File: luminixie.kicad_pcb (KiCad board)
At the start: 2 copper layers, 162.6 x 50.8 mm, 31 parts, among them J1 Conn_01x03_Female, U1 ESP32-MINIKIT, U2 HV-POWER, U3 HV5530_PLCC, U4 HV5530_PLCC

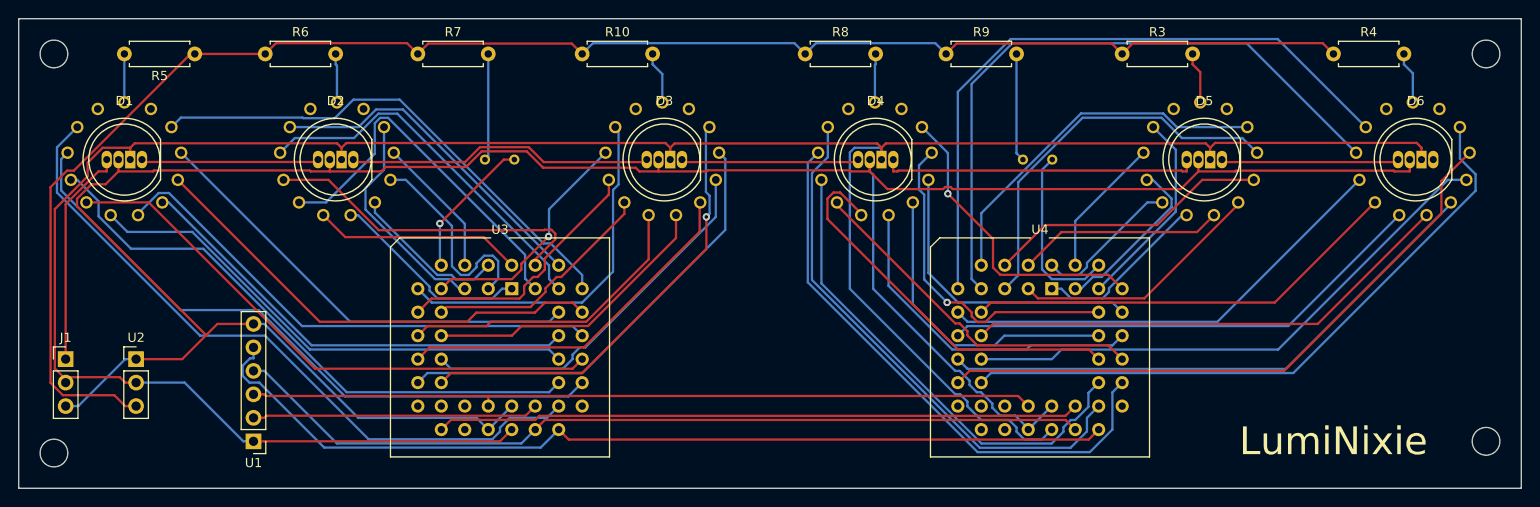
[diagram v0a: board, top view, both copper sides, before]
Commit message: Voltage divider for IN-3
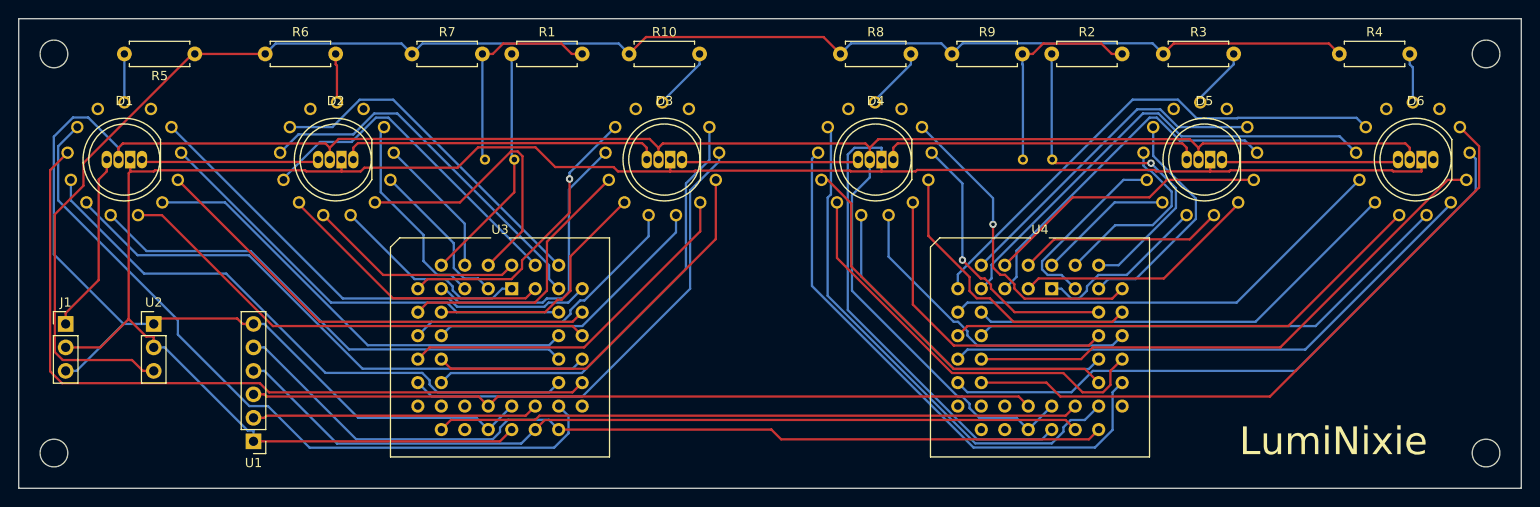
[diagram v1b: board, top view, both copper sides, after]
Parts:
- removed REF** (x4): MountingHole_3mm, MountingHole:MountingHole_3mm
- added R1: ?, Resistor_THT:R_Axial_DIN0207_L6.3mm_D2.5mm_P7.62mm_Horizontal, F.Cu at (133.3, 62.2)
- added R2: ?, Resistor_THT:R_Axial_DIN0207_L6.3mm_D2.5mm_P7.62mm_Horizontal, F.Cu at (191.8, 62.2)
- added REF1: MountingHole_3mm, MountingHole:MountingHole_3mm, F.Cu at (83.8, 62.2)
- added REF2: MountingHole_3mm, MountingHole:MountingHole_3mm, F.Cu at (83.8, 105.4)
- added REF5: MountingHole_3mm, MountingHole:MountingHole_3mm, F.Cu at (238.8, 62.2)
- added REF6: MountingHole_3mm, MountingHole:MountingHole_3mm, F.Cu at (238.8, 105.4)
- R7, R9: value 150K -> ?
- moved R10 5.08 mm to (146.1, 62.2)
- moved R3 4.45 mm to (203.8, 62.2)
- moved U2 4.26 mm to (94.6, 91.4)
- moved J1 3.81 mm to (85.1, 91.4)
- moved R8 3.81 mm to (168.9, 62.2)
- moved R4 0.63 mm to (222.9, 62.2)
- moved R7 0.63 mm to (122.6, 62.2)
- moved R9 0.63 mm to (181.0, 62.2)
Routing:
- net Net-(N6-Pad2): track 70.9 -> 51.0 mm
- net Net-(N8-PadK): track 19.5 -> 39.2 mm, vias 0 -> 1
- net Net-(N6-Pad1): track 71.7 -> 54.8 mm
- net Net-(N2-Pad7): track 17.0 -> 31.8 mm
- net Net-(N1-Pad2): track 70.6 -> 83.4 mm
- net Net-(N7-PadA): track 11.6 -> 23.3 mm
- net Net-(N8-PadA): track 11.7 -> 23.2 mm
- net Net-(N7-PadK): track 15.5 -> 26.2 mm, vias 1 -> 0
- net Net-(N2-Pad4): track 40.4 -> 30.4 mm
- net Net-(N4-Pad3): track 52.3 -> 43.1 mm
- net +5V: track 276.5 -> 285.1 mm
- net GND: track 281.5 -> 273.2 mm
- net Net-(N3-Pad1): track 39.2 -> 31.7 mm, vias 0 -> 1
- net Net-(N4-Pad4): track 38.3 -> 45.3 mm
- net Net-(N2-Pad8): track 23.3 -> 17.0 mm
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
